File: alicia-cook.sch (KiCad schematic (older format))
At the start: 109 parts, among them J1 02x05, J2 02x05, SW1 switch, SW10 switch, SW11 switch, SW12 switch, SW13 switch, SW14 switch, SW15 switch, SW16 switch, SW17 switch, SW18 switch, SW19 switch, SW2 switch, SW20 switch, SW21 switch, SW22 switch, SW23 switch, SW24 switch, SW3 switch, SW4 switch, SW5 switch, SW6 switch, SW7 switch, SW8 switch, SW9 switch, U1 ProMicro

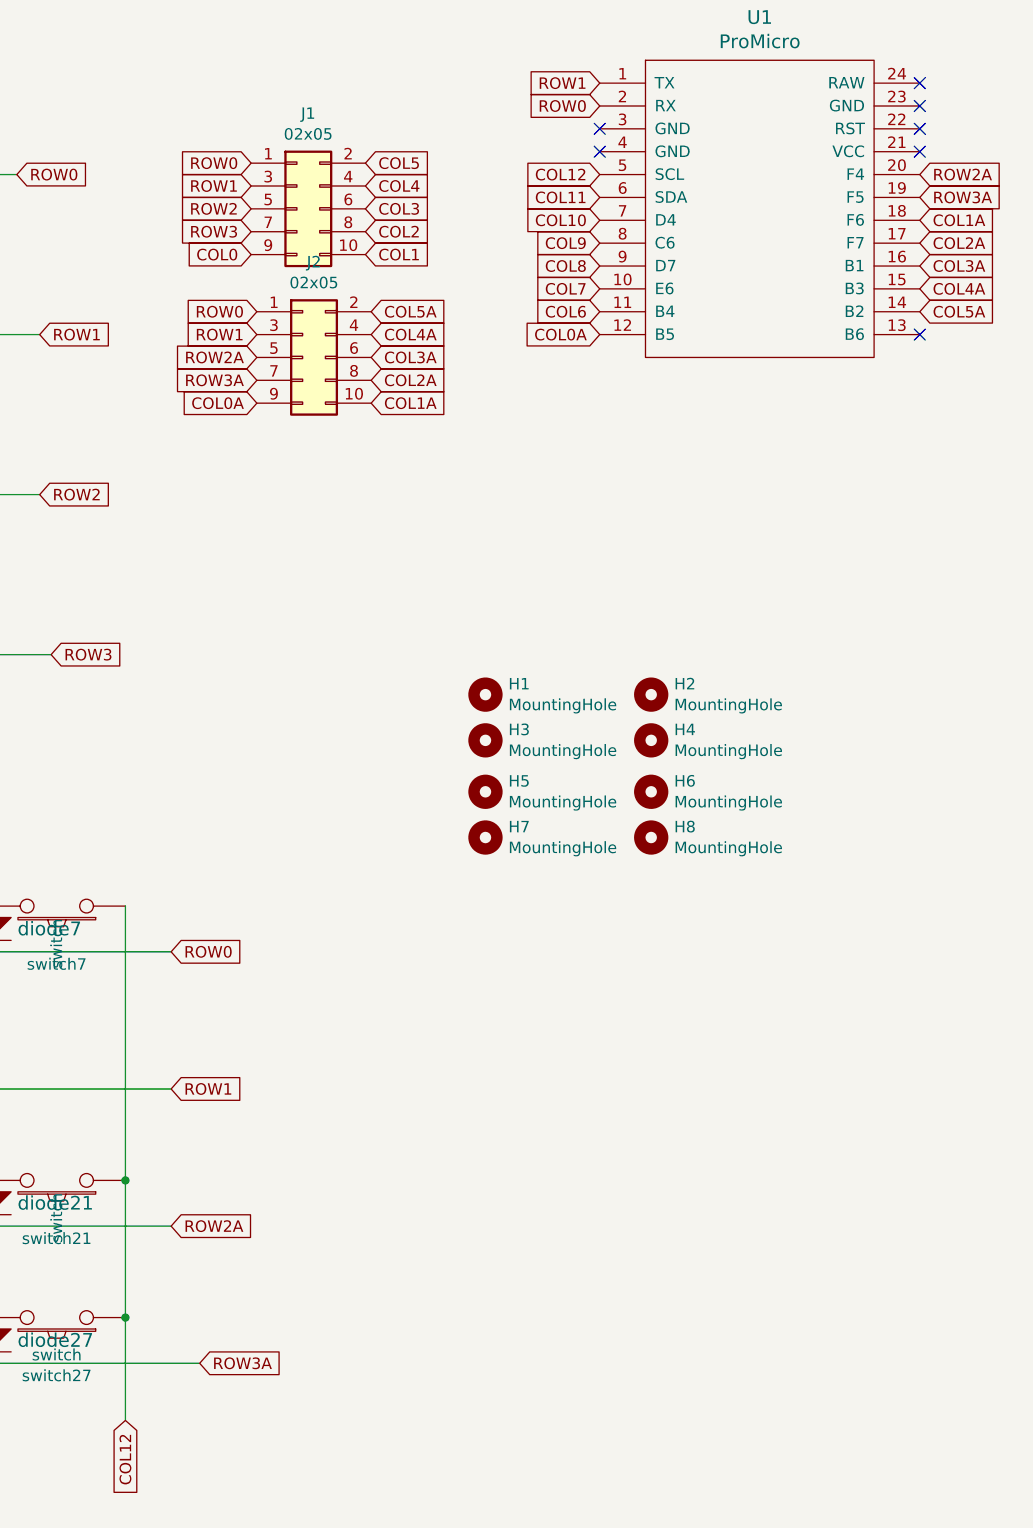
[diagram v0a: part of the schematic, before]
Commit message: some route fixes.
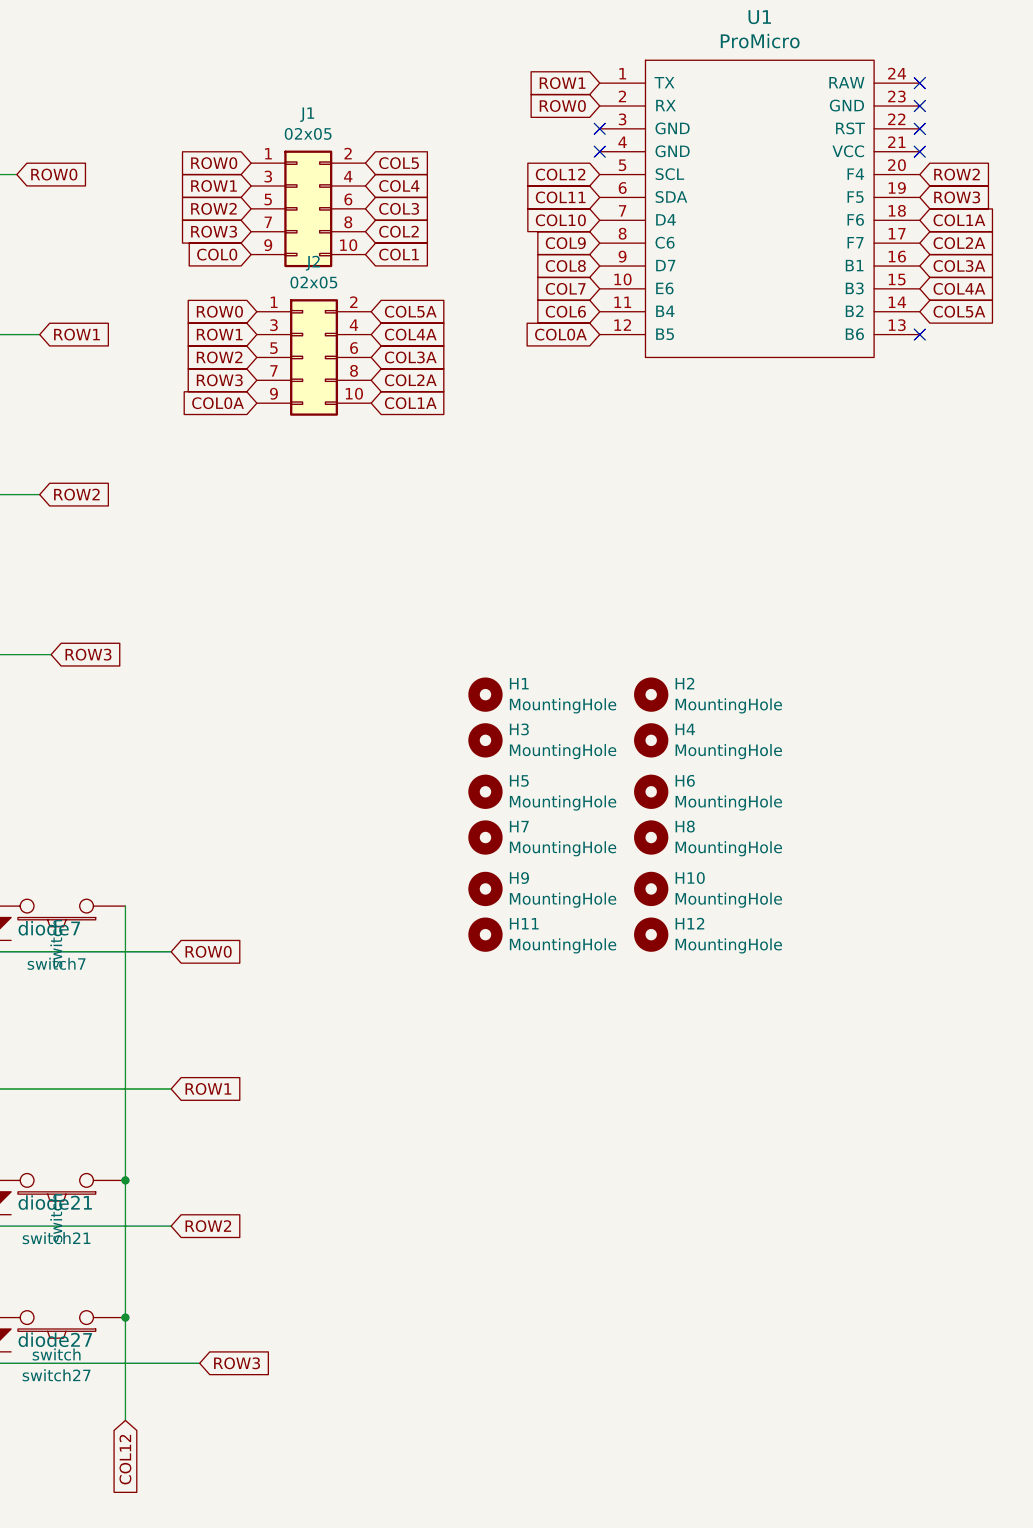
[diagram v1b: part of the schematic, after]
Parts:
- added H10, H11, H12, H9: MountingHole, footprints:hole-three, symbol mechanical:MountingHole
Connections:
- net ROW2A is gone; now on net ROW2: J2.5 (Pin_5), U1.20 (F4), diode15.1, diode16.1, diode17.1, diode18.1, diode19.1, diode20.1, diode21.1
- net ROW3A is gone; now on net ROW3: J2.7 (Pin_7), U1.19 (F5), diode22.1, diode24.1, diode25.1, diode26.1, diode27.1
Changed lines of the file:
@@
 NoConn ~ 10225 950
 Text GLabel 10225 1250 2    50   Input ~ 0
-ROW3A
+ROW3
 Text GLabel 10225 1150 2    50   Input ~ 0
-ROW2A
+ROW2
 Text GLabel 8825 750  0    50   Input ~ 0
 ROW1
@@
 ROW1
 Text GLabel 6950 5750 2    50   Input ~ 0
-ROW2A
+ROW2
 Text GLabel 7075 6350 2    50   Input ~ 0
-ROW3A
+ROW3
 Text GLabel 1350 6600 3    50   Input ~ 0
 COL6
@@
 ROW0
 Text GLabel 7325 1950 0    50   Input ~ 0
-ROW2A
+ROW2
 Text GLabel 7325 2050 0    50   Input ~ 0
-ROW3A
+ROW3
 Text GLabel 7800 1500 2    50   Input ~ 0
 COL1
@@
 	1    0    0    -1
 $EndComp
+$Comp
+L mechanical:MountingHole H9
+U 1 1 60085A62
+P 8325 4275
+F 0 "H9" H 8425 4321 50  0000 L CNN
+F 1 "MountingHole" H 8425 4230 50  0000 L CNN
+F 2 "footprints:hole-three" H 8325 4275 50  0001 C CNN
+F 3 "~" H 8325 4275 50  0001 C CNN
+	1    8325 4275
+	1    0    0    -1
+$EndComp
+$Comp
+L mechanical:MountingHole H11
+U 1 1 60085C68
+P 8325 4475
+F 0 "H11" H 8425 4521 50  0000 L CNN
+F 1 "MountingHole" H 8425 4430 50  0000 L CNN
+F 2 "footprints:hole-three" H 8325 4475 50  0001 C CNN
+F 3 "~" H 8325 4475 50  0001 C CNN
+	1    8325 4475
+	1    0    0    -1
+$EndComp
+$Comp
+L mechanical:MountingHole H10
+U 1 1 60085C72
+P 9050 4275
+F 0 "H10" H 9150 4321 50  0000 L CNN
+F 1 "MountingHole" H 9150 4230 50  0000 L CNN
+F 2 "footprints:hole-three" H 9050 4275 50  0001 C CNN
+F 3 "~" H 9050 4275 50  0001 C CNN
+	1    9050 4275
+	1    0    0    -1
+$EndComp
+$Comp
+L mechanical:MountingHole H12
+U 1 1 60085C7C
+P 9050 4475
+F 0 "H12" H 9150 4521 50  0000 L CNN
+F 1 "MountingHole" H 9150 4430 50  0000 L CNN
+F 2 "footprints:hole-three" H 9050 4475 50  0001 C CNN
+F 3 "~" H 9050 4475 50  0001 C CNN
+	1    9050 4475
+	1    0    0    -1
+$EndComp

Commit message: 3d models.
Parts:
- D1, D10, D11, D12, D13, D14, D15, D16, D17, D18, D19, D2, D20, D21, D22, D23, D3, D4, D5, D6, D7, D8, D9, diode1, diode10, diode11, diode12, diode13, diode15, diode16, diode17, diode18, diode19, diode2, diode20, diode21, diode22, diode24, diode25, diode26, diode27, diode3, diode4, diode5, diode6, diode7, diode8, diode9: footprint footprints:diode-vertical -> footprints:diode
- switch25: footprint footprints:15u-minimal -> footprints:1u-minimal
